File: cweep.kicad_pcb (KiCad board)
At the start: 2 copper layers, 106.6 x 82.7 mm, 57 parts

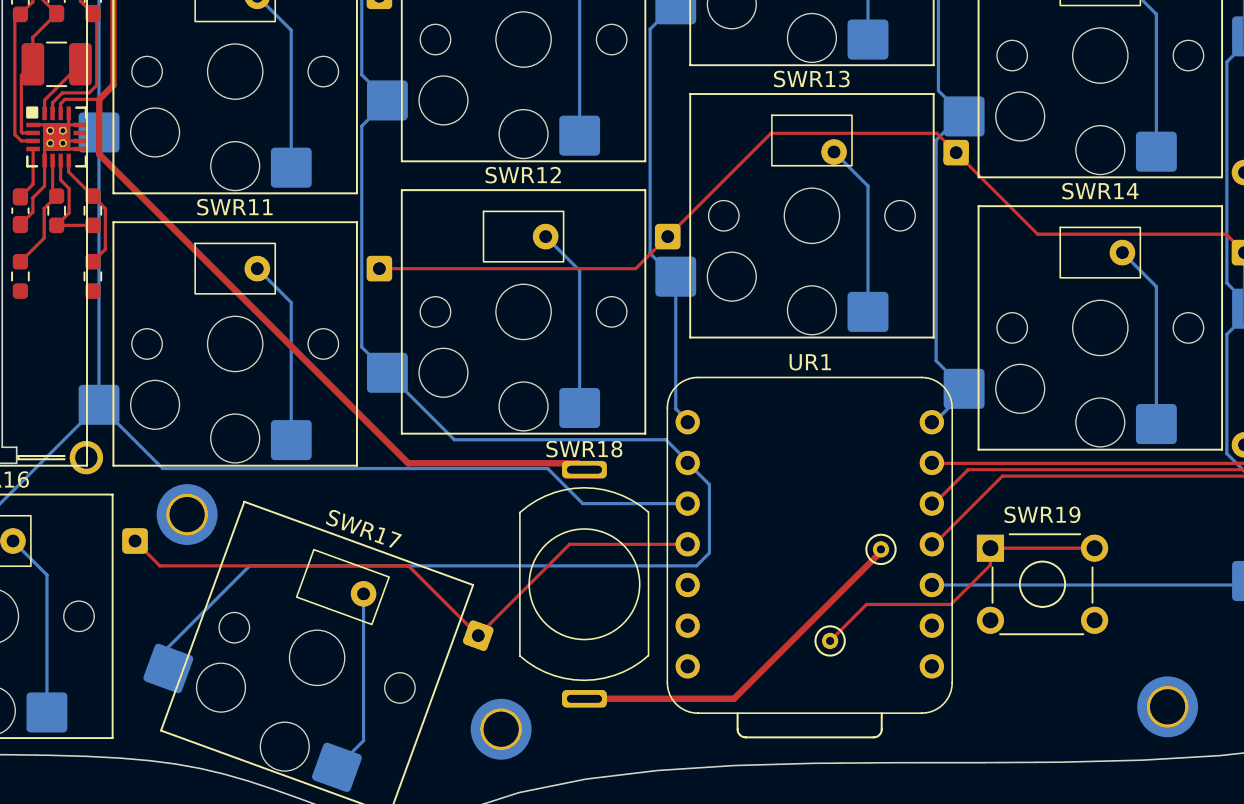
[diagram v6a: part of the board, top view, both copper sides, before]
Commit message: fix: visually align power and reset switches
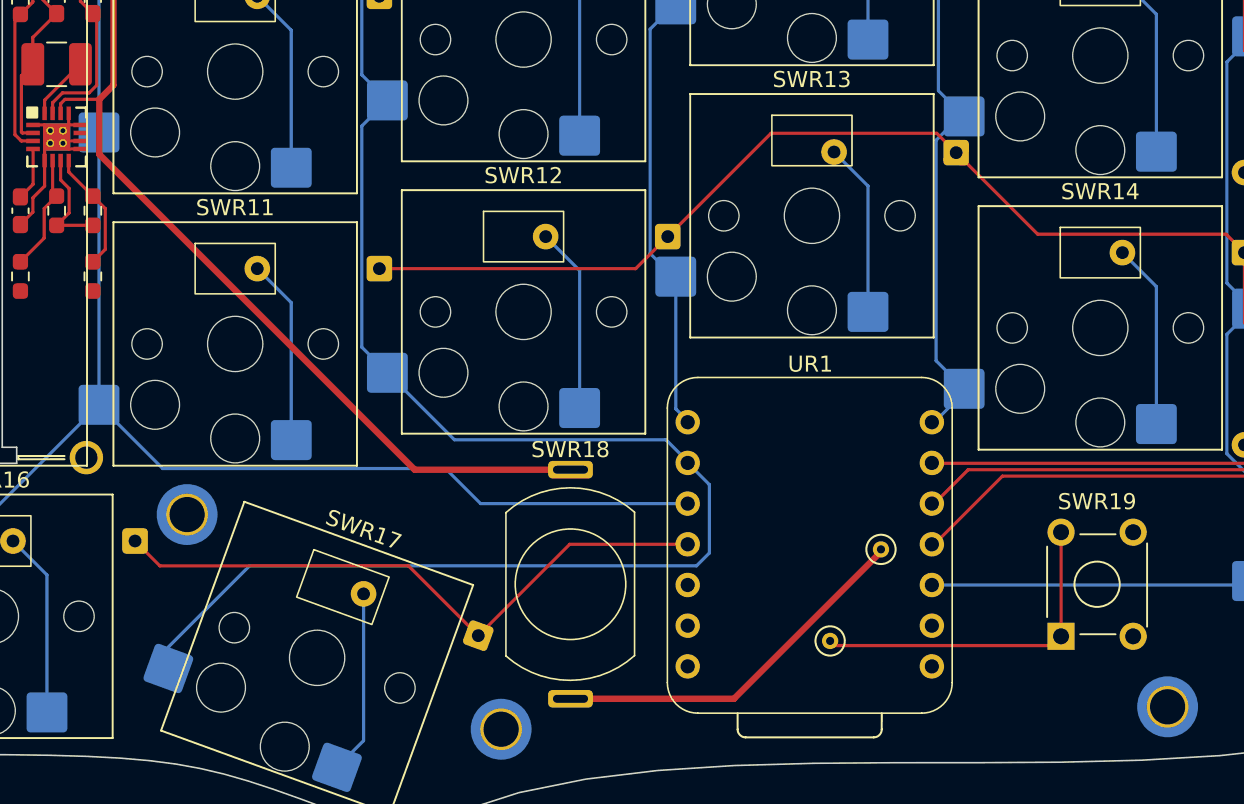
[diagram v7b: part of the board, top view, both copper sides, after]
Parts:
- moved SWR19 7.05 mm to (238.6, 103.2), turned to 90 degrees
- moved SWR18 0.87 mm to (207.9, 100.0)
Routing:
- net Net-(UR1-RESET): track 19.5 -> 21.3 mm
- net Net-(SWR18-A): track 22.5 -> 23.3 mm
- net /VBATR: track 67.7 -> 66.8 mm

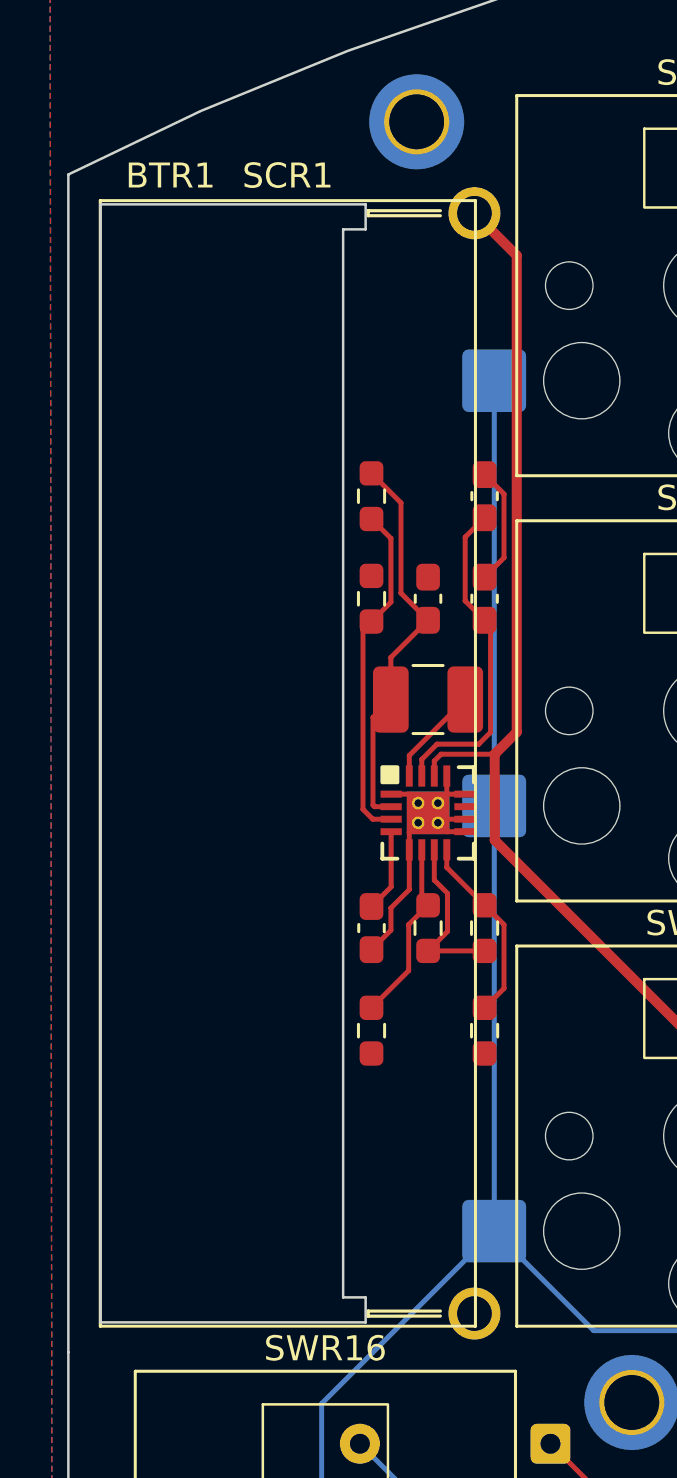
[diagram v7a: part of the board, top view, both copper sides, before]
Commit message: fix: join solar ground zone and avoid silkscreen clipping
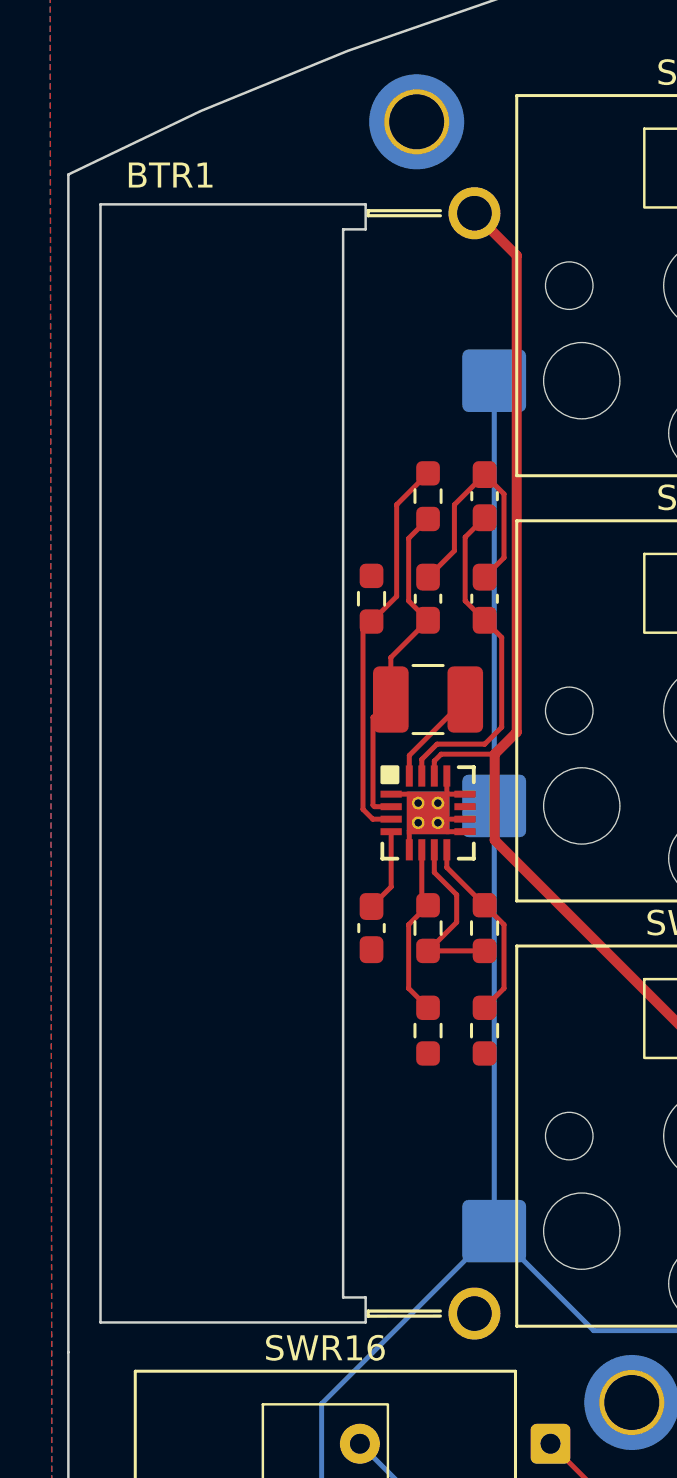
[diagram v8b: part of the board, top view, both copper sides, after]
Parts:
- moved ROCR2 2.26 mm to (175.9, 59.4), turned to -90 degrees
- moved ROVR1 2.26 mm to (175.9, 80.8)
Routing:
- net Net-(SCR1-+): track 15.9 -> 13.7 mm
- net Net-(UR2-VOC_SAMP): track 13.7 -> 15.8 mm
- net Net-(UR2-VSTOR): track 13.2 -> 13.7 mm
